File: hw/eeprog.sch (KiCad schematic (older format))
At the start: 6 parts, among them U1 74HC595, U2 74HC595, U3 74HC595, U4 28C256, U5 74HC165

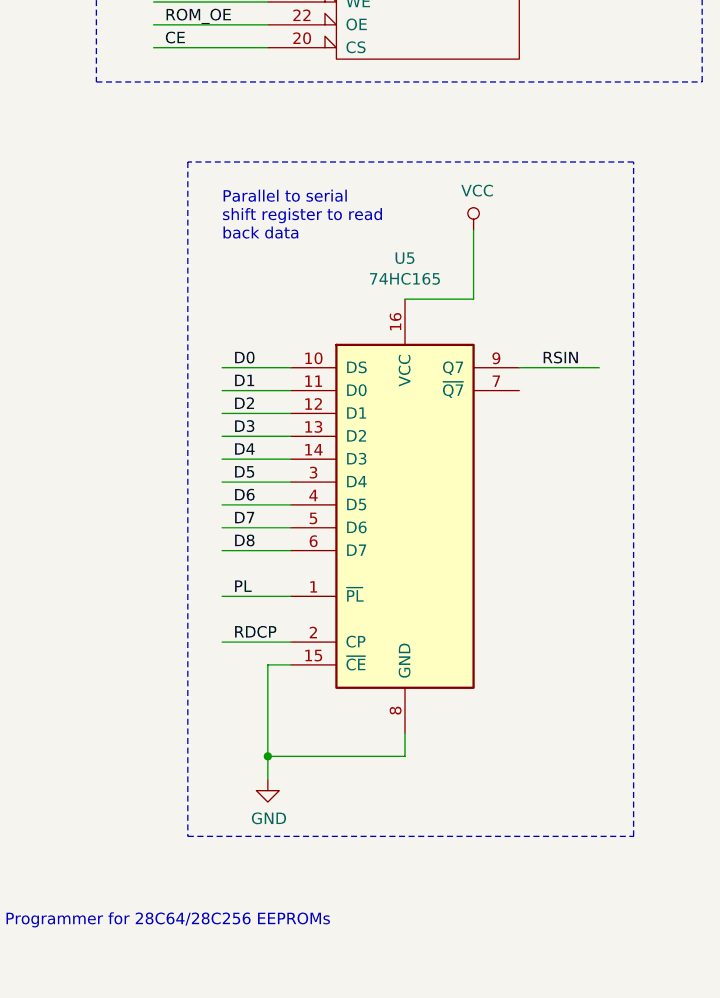
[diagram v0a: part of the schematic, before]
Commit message: fix inputs to 74HC165
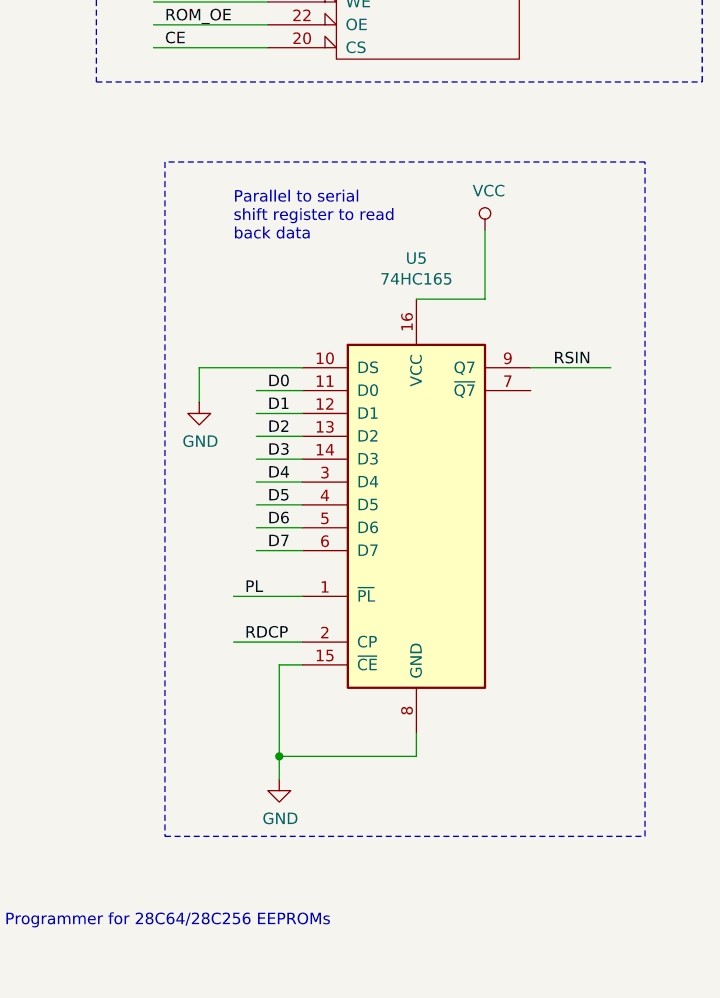
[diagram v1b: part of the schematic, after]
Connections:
- net labels removed: D8
- wire segments 119 -> 120
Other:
- moved on the sheet: U5
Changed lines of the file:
@@
 L 74xx:74LS165 U5
 U 1 1 5CF987FE
-P 8200 5100
-F 0 "U5" H 8200 6178 50  0000 C CNN
-F 1 "74HC165" H 8200 6087 50  0000 C CNN
-F 2 "" H 8200 5100 50  0001 C CNN
-F 3 "" H 8200 5100 50  0001 C CNN
-	1    8200 5100
-	1    0    0    -1
-$EndComp
-Wire Wire Line
-	7700 4500 7400 4500
-Wire Wire Line
-	7700 4600 7400 4600
-Wire Wire Line
-	7700 4700 7400 4700
-Wire Wire Line
-	7700 4800 7400 4800
-Wire Wire Line
-	7700 4900 7400 4900
-Wire Wire Line
-	7700 5000 7400 5000
-Wire Wire Line
-	7700 5100 7400 5100
-Wire Wire Line
-	7700 5200 7400 5200
-Wire Wire Line
-	7700 5300 7400 5300
-Text Label 7450 4500 0    50   ~ 0
+P 8250 5100
+F 0 "U5" H 8250 6178 50  0000 C CNN
+F 1 "74HC165" H 8250 6087 50  0000 C CNN
+F 2 "" H 8250 5100 50  0001 C CNN
+F 3 "" H 8250 5100 50  0001 C CNN
+	1    8250 5100
+	1    0    0    -1
+$EndComp
+Wire Wire Line
+	7750 4600 7550 4600
+Wire Wire Line
+	7750 4700 7550 4700
+Wire Wire Line
+	7750 4800 7550 4800
+Wire Wire Line
+	7750 4900 7550 4900
+Wire Wire Line
+	7750 5000 7550 5000
+Wire Wire Line
+	7750 5100 7550 5100
+Wire Wire Line
+	7750 5200 7550 5200
+Wire Wire Line
+	7750 5300 7550 5300
+Text Label 7600 4600 0    50   ~ 0
 D0
-Text Label 7450 4600 0    50   ~ 0
+Text Label 7600 4700 0    50   ~ 0
 D1
-Text Label 7450 4700 0    50   ~ 0
+Text Label 7600 4800 0    50   ~ 0
 D2
-Text Label 7450 4800 0    50   ~ 0
+Text Label 7600 4900 0    50   ~ 0
 D3
-Text Label 7450 4900 0    50   ~ 0
+Text Label 7600 5000 0    50   ~ 0
 D4
-Text Label 7450 5000 0    50   ~ 0
+Text Label 7600 5100 0    50   ~ 0
 D5
-Text Label 7450 5100 0    50   ~ 0
+Text Label 7600 5200 0    50   ~ 0
 D6
-Text Label 7450 5200 0    50   ~ 0
+Text Label 7600 5300 0    50   ~ 0
 D7
-Text Label 7450 5300 0    50   ~ 0
-D8
-Wire Wire Line
-	7700 5800 7600 5800
-Wire Wire Line
-	7600 5800 7600 6200
+Wire Wire Line
+	7750 5800 7650 5800
+Wire Wire Line
+	7650 5800 7650 6200
 $Comp
 L power:GND #PWR?
 U 1 1 5CFAEB9E
-P 7600 6300
-F 0 "#PWR?" H 7600 6050 50  0001 C CNN
-F 1 "GND" H 7605 6127 50  0000 C CNN
-F 2 "" H 7600 6300 50  0001 C CNN
-F 3 "" H 7600 6300 50  0001 C CNN
-	1    7600 6300
-	1    0    0    -1
-$EndComp
-Wire Wire Line
-	7700 5500 7400 5500
-Text Label 7450 5500 0    50   ~ 0
+P 7650 6300
+F 0 "#PWR?" H 7650 6050 50  0001 C CNN
+F 1 "GND" H 7655 6127 50  0000 C CNN
+F 2 "" H 7650 6300 50  0001 C CNN
+F 3 "" H 7650 6300 50  0001 C CNN
+	1    7650 6300
+	1    0    0    -1
+$EndComp
+Wire Wire Line
+	7750 5500 7450 5500
+Text Label 7500 5500 0    50   ~ 0
 PL
 Wire Wire Line
-	7700 5700 7400 5700
-Text Label 7450 5700 0    50   ~ 0
+	7750 5700 7450 5700
+Text Label 7500 5700 0    50   ~ 0
 RDCP
 Wire Wire Line
-	8200 6100 8200 6200
-Wire Wire Line
-	8200 6200 7600 6200
-Connection ~ 7600 6200
-Wire Wire Line
-	7600 6200 7600 6300
-Wire Wire Line
-	8700 4500 9050 4500
-Text Label 8800 4500 0    50   ~ 0
+	8250 6100 8250 6200
+Wire Wire Line
+	8250 6200 7650 6200
+Connection ~ 7650 6200
+Wire Wire Line
+	7650 6200 7650 6300
+Wire Wire Line
+	8750 4500 9100 4500
+Text Label 8850 4500 0    50   ~ 0
 RSIN
 Wire Wire Line
@@
 RSIN
 Wire Wire Line
-	8200 4200 8500 4200
-Wire Wire Line
-	8500 4200 8500 3900
+	8250 4200 8550 4200
+Wire Wire Line
+	8550 4200 8550 3900
 $Comp
 L power:VCC #PWR?
 U 1 1 5CFD9C61
-P 8500 3900
-F 0 "#PWR?" H 8500 3750 50  0001 C CNN
-F 1 "VCC" H 8517 4073 50  0000 C CNN
-F 2 "" H 8500 3900 50  0001 C CNN
-F 3 "" H 8500 3900 50  0001 C CNN
-	1    8500 3900
+P 8550 3900
+F 0 "#PWR?" H 8550 3750 50  0001 C CNN
+F 1 "VCC" H 8567 4073 50  0000 C CNN
+F 2 "" H 8550 3900 50  0001 C CNN
+F 3 "" H 8550 3900 50  0001 C CNN
+	1    8550 3900
 	1    0    0    -1
 $EndComp
@@
 Wire Notes Line
 	9500 750  6850 750
-Text Notes 7400 3950 0    50   ~ 0
+Text Notes 7450 3950 0    50   ~ 0
 Parallel to serial\nshift register to read\nback data
 Wire Notes Line
-	7250 3600 7250 6550
-Wire Notes Line
-	7250 6550 9200 6550
-Wire Notes Line
-	9200 6550 9200 3600
-Wire Notes Line
-	9200 3600 7250 3600
+	7150 3600 7150 6550
+Wire Notes Line
+	7150 6550 9250 6550
+Wire Notes Line
+	9250 6550 9250 3600
+Wire Notes Line
+	9250 3600 7150 3600
+Wire Wire Line
+	7750 4500 7300 4500
+Wire Wire Line
+	7300 4500 7300 4650
+$Comp
+L power:GND #PWR?
+U 1 1 5CFA4886
+P 7300 4650
+F 0 "#PWR?" H 7300 4400 50  0001 C CNN
+F 1 "GND" H 7305 4477 50  0000 C CNN
+F 2 "" H 7300 4650 50  0001 C CNN
+F 3 "" H 7300 4650 50  0001 C CNN
+	1    7300 4650
+	1    0    0    -1
+$EndComp
 $EndSCHEMATC

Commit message: eliminate AOE, rename signals for clarity
AOE is unnecessary because the address outputs should
always be active.

Renamed some signals on the ROM and the 74HC165 to
give them a common prefix.
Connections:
- net labels added: RDIN, RDPL, ROM_CE, ROM_WE
- net labels removed: AOE, CE, PL, RSIN, WE
- wire segments 120 -> 121
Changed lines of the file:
@@
 	3250 4600 2900 4600
 Text Label 2950 4500 0    50   ~ 0
-CE
+ROM_CE
 Text Label 2950 4600 0    50   ~ 0
-WE
+ROM_WE
 Wire Wire Line
 	4600 2000 4200 2000
-Text Label 4250 2000 0    50   ~ 0
-AOE
-Wire Wire Line
-	4600 4250 4200 4250
-Text Label 4250 4250 0    50   ~ 0
-AOE
 Wire Wire Line
 	4600 6750 4200 6750
 Text Label 4250 6750 0    50   ~ 0
 DOE
-Wire Wire Line
-	3250 4700 2900 4700
-Text Label 2950 4700 0    50   ~ 0
-AOE
 Text Notes 6450 6950 0    50   ~ 0
 Programmer for 28C64/28C256 EEPROMs
@@
 	7600 3100 7100 3100
 Text Label 7150 2900 0    50   ~ 0
-WE
+ROM_WE
 Text Label 7150 3100 0    50   ~ 0
-CE
-Wire Wire Line
-	1500 3300 1150 3300
-Text Label 1200 3300 0    50   ~ 0
+ROM_CE
+Wire Wire Line
+	3250 4800 2900 4800
+Text Label 2950 4800 0    50   ~ 0
 ROM_OE
 Text Label 7150 3000 0    50   ~ 0
@@
 	7750 5500 7450 5500
 Text Label 7500 5500 0    50   ~ 0
-PL
+RDPL
 Wire Wire Line
 	7750 5700 7450 5700
@@
 	8750 4500 9100 4500
 Text Label 8850 4500 0    50   ~ 0
-RSIN
-Wire Wire Line
-	3250 4800 2900 4800
-Text Label 2950 4800 0    50   ~ 0
+RDIN
+Wire Wire Line
+	3250 4700 2900 4700
+Text Label 2950 4700 0    50   ~ 0
 DOE
 Wire Wire Line
+	1500 3300 1150 3300
+Wire Wire Line
 	1500 3400 1150 3400
 Wire Wire Line
 	1500 3500 1150 3500
-Wire Wire Line
-	1500 3600 1150 3600
+Text Label 1200 3300 0    50   ~ 0
+RDPL
 Text Label 1200 3400 0    50   ~ 0
-PL
+RDCP
 Text Label 1200 3500 0    50   ~ 0
-RDCP
-Text Label 1200 3600 0    50   ~ 0
-RSIN
+RDIN
 Wire Wire Line
 	8250 4200 8550 4200
@@
 	1    0    0    -1
 $EndComp
+Wire Wire Line
+	4200 2000 4200 2250
+$Comp
+L power:GND #PWR?
+U 1 1 5CF879D2
+P 4200 2250
+F 0 "#PWR?" H 4200 2000 50  0001 C CNN
+F 1 "GND" H 4205 2077 50  0000 C CNN
+F 2 "" H 4200 2250 50  0001 C CNN
+F 3 "" H 4200 2250 50  0001 C CNN
+	1    4200 2250
+	1    0    0    -1
+$EndComp
+Wire Wire Line
+	4600 4250 4200 4250
+Wire Wire Line
+	4200 4250 4200 4500
+$Comp
+L power:GND #PWR?
+U 1 1 5CF87A58
+P 4200 4500
+F 0 "#PWR?" H 4200 4250 50  0001 C CNN
+F 1 "GND" H 4205 4327 50  0000 C CNN
+F 2 "" H 4200 4500 50  0001 C CNN
+F 3 "" H 4200 4500 50  0001 C CNN
+	1    4200 4500
+	1    0    0    -1
+$EndComp

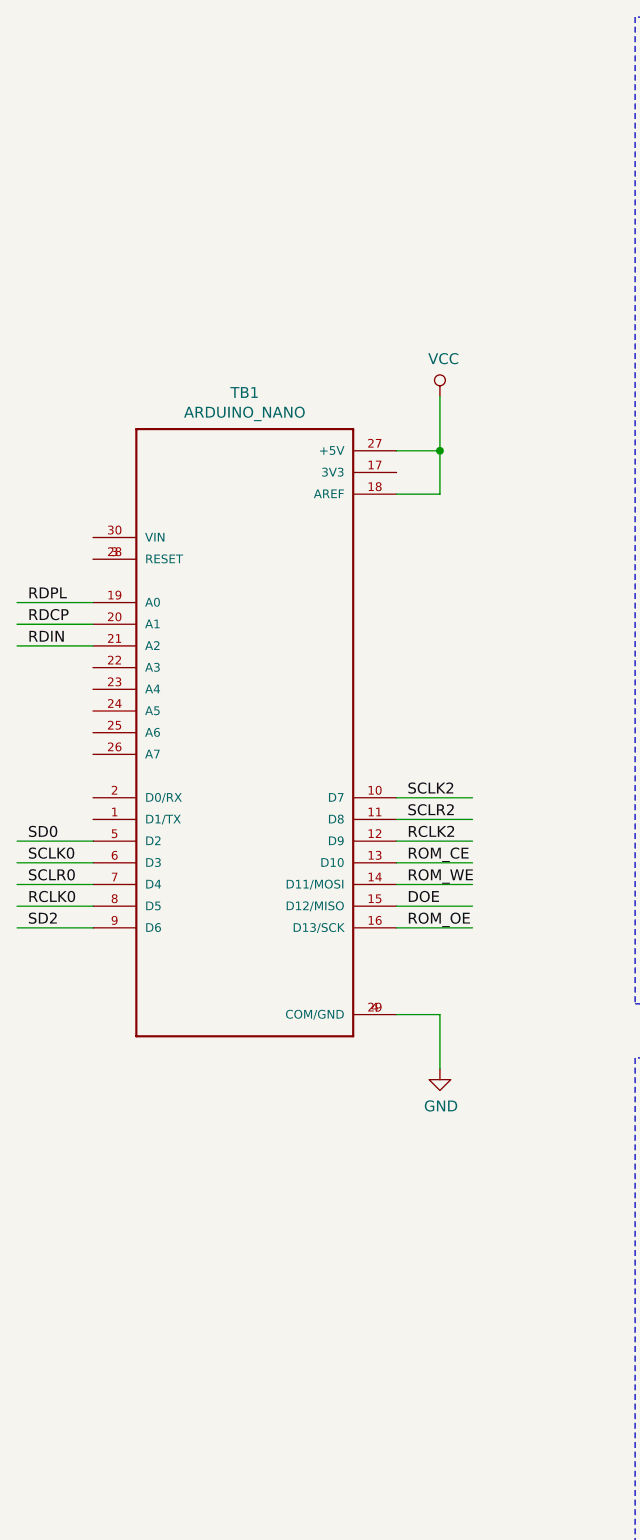
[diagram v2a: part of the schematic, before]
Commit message: add pull-up resistors on data lines
This ensures that the inputs to the EEPROM and
74HC165 are never floating.
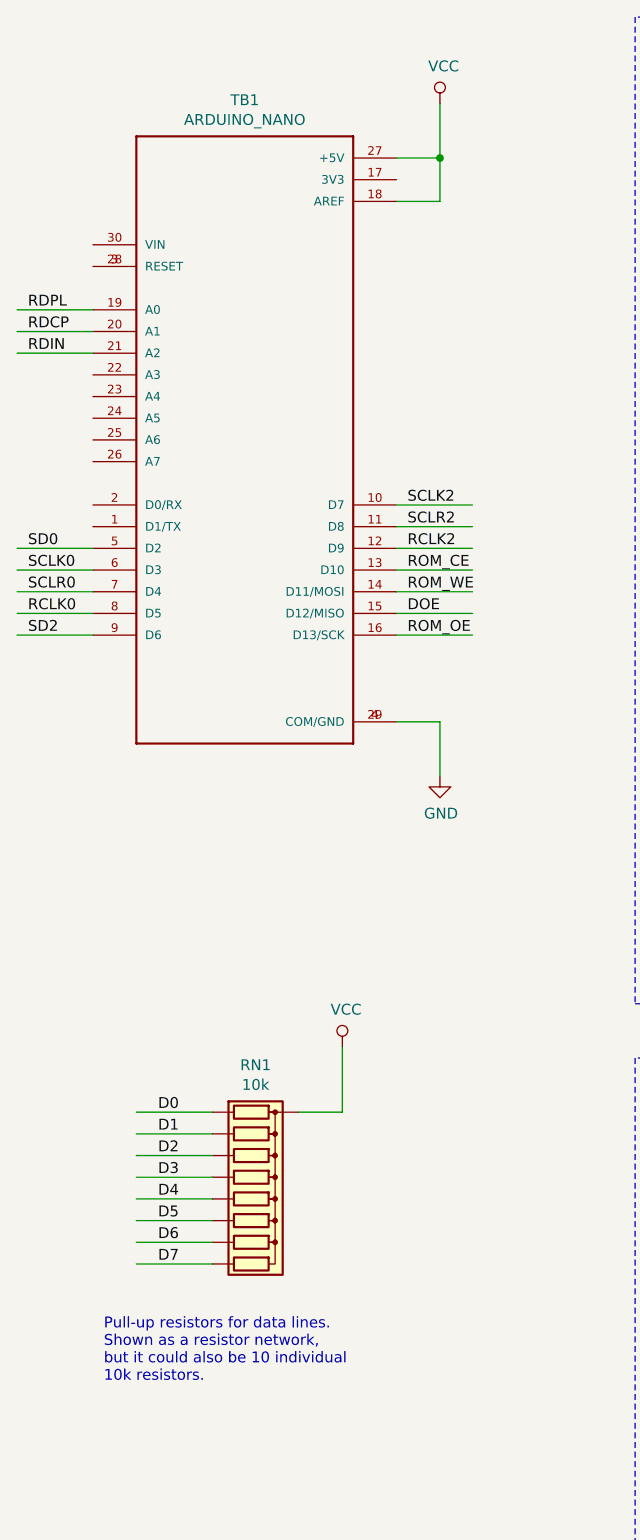
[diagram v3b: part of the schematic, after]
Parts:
- added RN1: 10k, Resistors_THT:R_Array_SIP9, symbol device:R_Network08
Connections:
- wire segments 121 -> 131
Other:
- note added: "Pull-up resistors for data lines.\nShown as a resistor network,\nbut it could also be 10 individual\n10k resistors."
- moved on the sheet: TB1
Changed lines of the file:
@@
 L ARDUINO_NANO:ARDUINO_NANO TB1
 U 1 1 5CF67873
-P 2200 3900
-F 0 "TB1" H 2200 5467 50  0000 C CNN
-F 1 "ARDUINO_NANO" H 2200 5376 50  0000 C CNN
-F 2 "SHIELD_ARDUINO_NANO" H 2200 3900 50  0001 L BNN
-F 3 "DFRobot" H 2200 3900 50  0001 L BNN
-F 4 "Dev.kit: Arduino; UART; ICSP, USB B mini, pin strips" H 2200 3900 50  0001 L BNN "Field4"
-F 5 "None" H 2200 3900 50  0001 L BNN "Field5"
-F 6 "None" H 2200 3900 50  0001 L BNN "Field6"
-F 7 "ARDUINO NANO" H 2200 3900 50  0001 L BNN "Field7"
-F 8 "Unavailable" H 2200 3900 50  0001 L BNN "Field8"
-	1    2200 3900
+P 2200 2550
+F 0 "TB1" H 2200 4117 50  0000 C CNN
+F 1 "ARDUINO_NANO" H 2200 4026 50  0000 C CNN
+F 2 "SHIELD_ARDUINO_NANO" H 2200 2550 50  0001 L BNN
+F 3 "DFRobot" H 2200 2550 50  0001 L BNN
+F 4 "Dev.kit: Arduino; UART; ICSP, USB B mini, pin strips" H 2200 2550 50  0001 L BNN "Field4"
+F 5 "None" H 2200 2550 50  0001 L BNN "Field5"
+F 6 "None" H 2200 2550 50  0001 L BNN "Field6"
+F 7 "ARDUINO NANO" H 2200 2550 50  0001 L BNN "Field7"
+F 8 "Unavailable" H 2200 2550 50  0001 L BNN "Field8"
+	1    2200 2550
 	1    0    0    -1
 $EndComp
@@
 L power:VCC #PWR?
 U 1 1 5CF6793D
-P 3100 2350
-F 0 "#PWR?" H 3100 2200 50  0001 C CNN
-F 1 "VCC" H 3117 2523 50  0000 C CNN
-F 2 "" H 3100 2350 50  0001 C CNN
-F 3 "" H 3100 2350 50  0001 C CNN
-	1    3100 2350
-	1    0    0    -1
-$EndComp
-Wire Wire Line
-	2900 2800 3100 2800
-Wire Wire Line
-	3100 2800 3100 2600
-Wire Wire Line
-	2900 2600 3100 2600
-Connection ~ 3100 2600
-Wire Wire Line
-	3100 2600 3100 2350
+P 3100 1000
+F 0 "#PWR?" H 3100 850 50  0001 C CNN
+F 1 "VCC" H 3117 1173 50  0000 C CNN
+F 2 "" H 3100 1000 50  0001 C CNN
+F 3 "" H 3100 1000 50  0001 C CNN
+	1    3100 1000
+	1    0    0    -1
+$EndComp
+Wire Wire Line
+	2900 1450 3100 1450
+Wire Wire Line
+	3100 1450 3100 1250
+Wire Wire Line
+	2900 1250 3100 1250
+Connection ~ 3100 1250
+Wire Wire Line
+	3100 1250 3100 1000
 $Comp
 L 74xx:74HC595 U1
@@
 $EndComp
 Wire Wire Line
-	2900 5200 3100 5200
-Wire Wire Line
-	3100 5200 3100 5450
+	2900 3850 3100 3850
+Wire Wire Line
+	3100 3850 3100 4100
 $Comp
 L power:GND #PWR?
 U 1 1 5CF6A4DB
-P 3100 5450
-F 0 "#PWR?" H 3100 5200 50  0001 C CNN
-F 1 "GND" H 3105 5277 50  0000 C CNN
-F 2 "" H 3100 5450 50  0001 C CNN
-F 3 "" H 3100 5450 50  0001 C CNN
-	1    3100 5450
-	1    0    0    -1
-$EndComp
-Wire Wire Line
-	1500 4400 1150 4400
-Wire Wire Line
-	1500 4500 1150 4500
-Wire Wire Line
-	1500 4700 1150 4700
-Wire Wire Line
-	1500 4600 1150 4600
-Text Label 1200 4400 0    50   ~ 0
+P 3100 4100
+F 0 "#PWR?" H 3100 3850 50  0001 C CNN
+F 1 "GND" H 3105 3927 50  0000 C CNN
+F 2 "" H 3100 4100 50  0001 C CNN
+F 3 "" H 3100 4100 50  0001 C CNN
+	1    3100 4100
+	1    0    0    -1
+$EndComp
+Wire Wire Line
+	1500 3050 1150 3050
+Wire Wire Line
+	1500 3150 1150 3150
+Wire Wire Line
+	1500 3350 1150 3350
+Wire Wire Line
+	1500 3250 1150 3250
+Text Label 1200 3050 0    50   ~ 0
 SD0
-Text Label 1200 4500 0    50   ~ 0
+Text Label 1200 3150 0    50   ~ 0
 SCLK0
-Text Label 1200 4700 0    50   ~ 0
+Text Label 1200 3350 0    50   ~ 0
 RCLK0
-Text Label 1200 4600 0    50   ~ 0
+Text Label 1200 3250 0    50   ~ 0
 SCLR0
 Wire Wire Line
@@
 RCLK2
 Wire Wire Line
-	2900 4200 3250 4200
-Wire Wire Line
-	2900 4300 3250 4300
-Wire Wire Line
-	2900 4400 3250 4400
-Text Label 2950 4200 0    50   ~ 0
+	2900 2850 3250 2850
+Wire Wire Line
+	2900 2950 3250 2950
+Wire Wire Line
+	2900 3050 3250 3050
+Text Label 2950 2850 0    50   ~ 0
 SCLK2
-Text Label 2950 4300 0    50   ~ 0
+Text Label 2950 2950 0    50   ~ 0
 SCLR2
-Text Label 2950 4400 0    50   ~ 0
+Text Label 2950 3050 0    50   ~ 0
 RCLK2
 Wire Wire Line
-	1150 4800 1500 4800
-Text Label 1200 4800 0    50   ~ 0
+	1150 3450 1500 3450
+Text Label 1200 3450 0    50   ~ 0
 SD2
 Wire Wire Line
@@
 $EndComp
 Wire Wire Line
-	3250 4500 2900 4500
-Wire Wire Line
-	3250 4600 2900 4600
-Text Label 2950 4500 0    50   ~ 0
+	3250 3150 2900 3150
+Wire Wire Line
+	3250 3250 2900 3250
+Text Label 2950 3150 0    50   ~ 0
 ROM_CE
-Text Label 2950 4600 0    50   ~ 0
+Text Label 2950 3250 0    50   ~ 0
 ROM_WE
 Wire Wire Line
@@
 ROM_CE
 Wire Wire Line
-	3250 4800 2900 4800
-Text Label 2950 4800 0    50   ~ 0
+	3250 3450 2900 3450
+Text Label 2950 3450 0    50   ~ 0
 ROM_OE
 Text Label 7150 3000 0    50   ~ 0
@@
 RDIN
 Wire Wire Line
-	3250 4700 2900 4700
-Text Label 2950 4700 0    50   ~ 0
+	3250 3350 2900 3350
+Text Label 2950 3350 0    50   ~ 0
 DOE
 Wire Wire Line
-	1500 3300 1150 3300
-Wire Wire Line
-	1500 3400 1150 3400
-Wire Wire Line
-	1500 3500 1150 3500
-Text Label 1200 3300 0    50   ~ 0
+	1500 1950 1150 1950
+Wire Wire Line
+	1500 2050 1150 2050
+Wire Wire Line
+	1500 2150 1150 2150
+Text Label 1200 1950 0    50   ~ 0
 RDPL
-Text Label 1200 3400 0    50   ~ 0
+Text Label 1200 2050 0    50   ~ 0
 RDCP
-Text Label 1200 3500 0    50   ~ 0
+Text Label 1200 2150 0    50   ~ 0
 RDIN
 Wire Wire Line
@@
 	1    0    0    -1
 $EndComp
+$Comp
+L device:R_Network08 RN1
+U 1 1 5CFC8FF9
+P 2250 6050
+F 0 "RN1" V 1633 6050 50  0000 C CNN
+F 1 "10k" V 1724 6050 50  0000 C CNN
+F 2 "Resistors_THT:R_Array_SIP9" V 2725 6050 50  0001 C CNN
+F 3 "" H 2250 6050 50  0001 C CNN
+	1    2250 6050
+	0    1    1    0
+$EndComp
+Wire Wire Line
+	2450 5650 2650 5650
+Wire Wire Line
+	2650 5650 2650 5350
+$Comp
+L power:VCC #PWR?
+U 1 1 5CFD929D
+P 2650 5350
+F 0 "#PWR?" H 2650 5200 50  0001 C CNN
+F 1 "VCC" H 2667 5523 50  0000 C CNN
+F 2 "" H 2650 5350 50  0001 C CNN
+F 3 "" H 2650 5350 50  0001 C CNN
+	1    2650 5350
+	1    0    0    -1
+$EndComp
+Wire Wire Line
+	2050 5650 1700 5650
+Wire Wire Line
+	2050 5750 1700 5750
+Wire Wire Line
+	2050 5850 1700 5850
+Wire Wire Line
+	2050 5950 1700 5950
+Wire Wire Line
+	2050 6050 1700 6050
+Wire Wire Line
+	2050 6150 1700 6150
+Wire Wire Line
+	2050 6250 1700 6250
+Wire Wire Line
+	2050 6350 1700 6350
+Text Label 1800 5650 0    50   ~ 0
+D0
+Text Label 1800 5750 0    50   ~ 0
+D1
+Text Label 1800 5850 0    50   ~ 0
+D2
+Text Label 1800 5950 0    50   ~ 0
+D3
+Text Label 1800 6050 0    50   ~ 0
+D4
+Text Label 1800 6150 0    50   ~ 0
+D5
+Text Label 1800 6250 0    50   ~ 0
+D6
+Text Label 1800 6350 0    50   ~ 0
+D7
+Text Notes 1550 6900 0    50   ~ 0
+Pull-up resistors for data lines.\nShown as a resistor network,\nbut it could also be 10 individual\n10k resistors.
 $EndSCHEMATC
